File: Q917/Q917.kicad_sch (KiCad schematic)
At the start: 6 parts, among them J1 Analog, J2 Digital

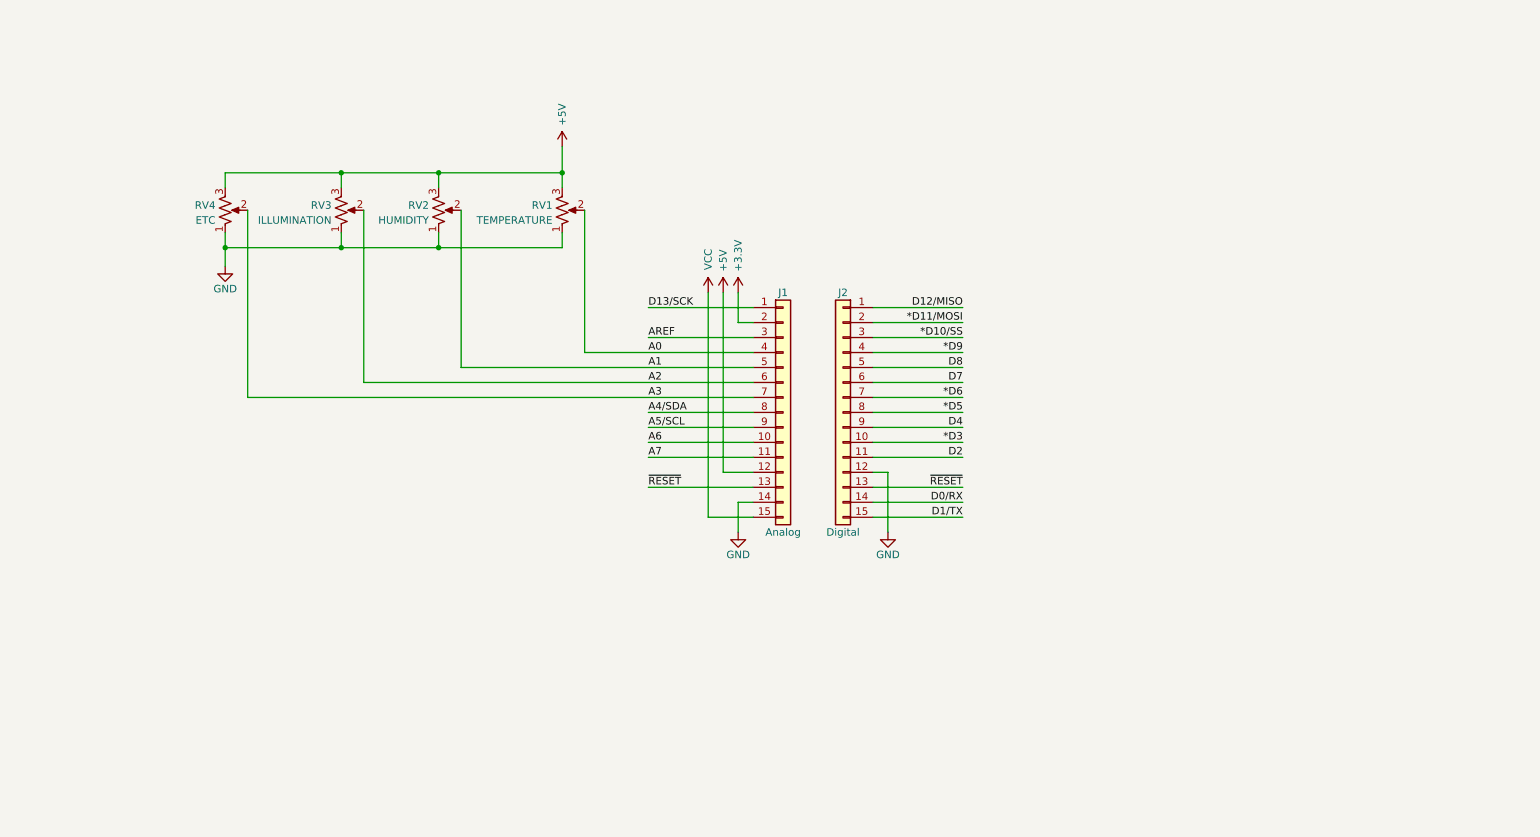
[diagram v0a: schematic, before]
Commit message: sche: コネクタ類に変更
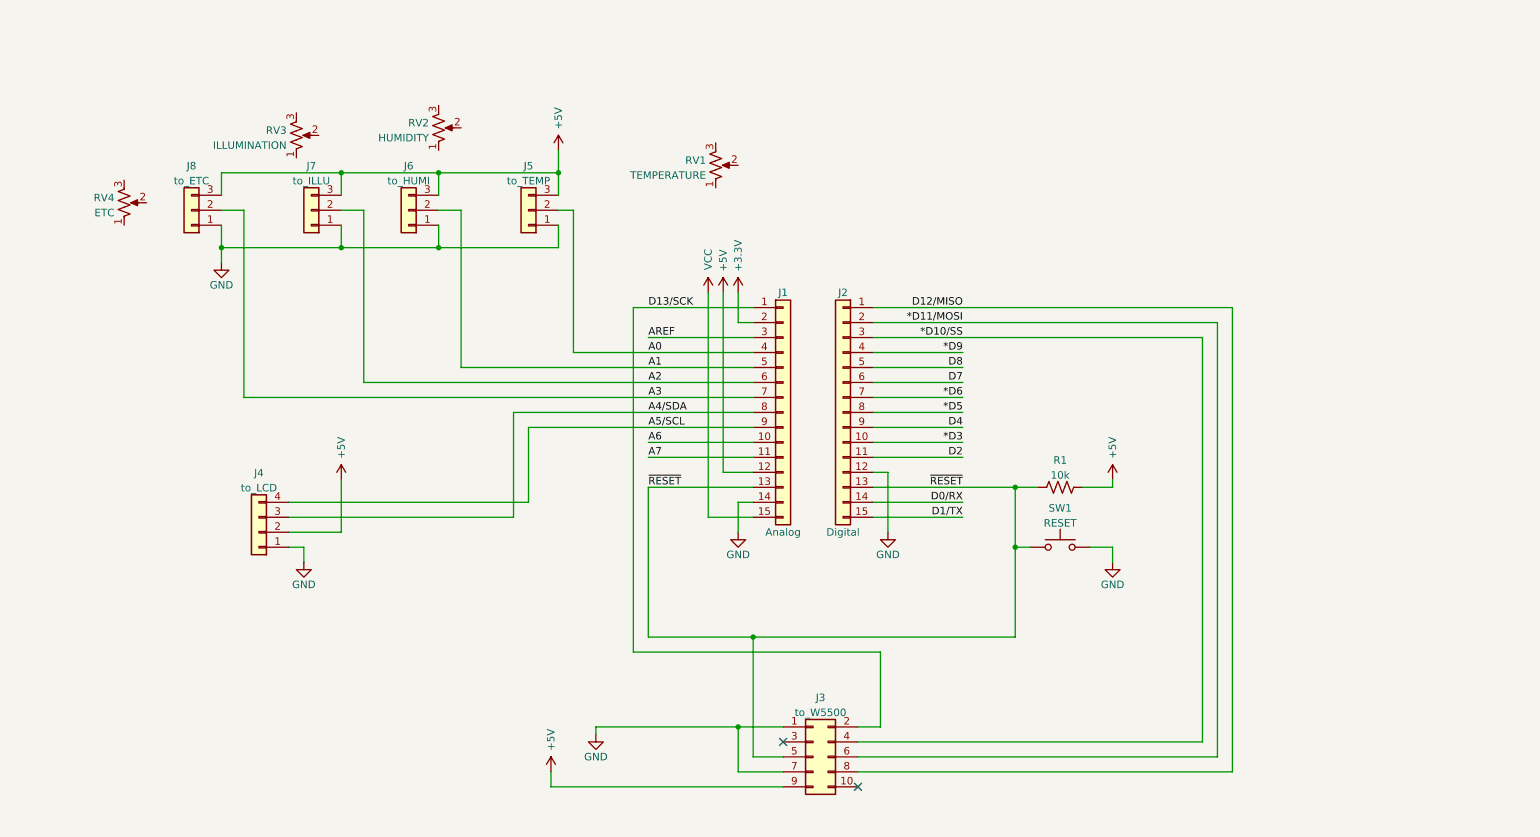
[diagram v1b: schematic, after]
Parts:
- added J3: to_W5500, Connector_PinHeader_2.54mm:PinHeader_2x05_P2.54mm_Vertical, symbol Connector_Generic:Conn_02x05_Odd_Even
- added J4: to_LCD, symbol Connector_Generic:Conn_01x04
- added J5: to_TEMP, Connector_JST:JST_XH_B3B-XH-A_1x03_P2.50mm_Vertical, symbol Connector_Generic:Conn_01x03
- added J6: to_HUMI, Connector_JST:JST_XH_B3B-XH-A_1x03_P2.50mm_Vertical, symbol Connector_Generic:Conn_01x03
- added J7: to_ILLU, Connector_JST:JST_XH_B3B-XH-A_1x03_P2.50mm_Vertical, symbol Connector_Generic:Conn_01x03
- added J8: to_ETC, Connector_JST:JST_XH_B3B-XH-A_1x03_P2.50mm_Vertical, symbol Connector_Generic:Conn_01x03
- added R1: 10k, symbol Device:R_US
- added SW1: RESET, symbol Switch:SW_Push
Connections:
- net *D10/SS: now also J3.4 (Pin_4)
- net *D11/MOSI: now also J3.6 (Pin_6)
- net +5V: now also J3.9 (Pin_9), J4.2 (Pin_2), J5.3 (Pin_3), J6.3 (Pin_3), J7.3 (Pin_3), J8.3 (Pin_3), R1.2; no longer RV1.3, RV2.3, RV3.3, RV4.3
- net A0: now also J5.2 (Pin_2); no longer RV1.2
- net A1: now also J6.2 (Pin_2); no longer RV2.2
- net A2: now also J7.2 (Pin_2); no longer RV3.2
- net A3: now also J8.2 (Pin_2); no longer RV4.2
- net A4/SDA: now also J4.3 (Pin_3)
- net A5/SCL: now also J4.4 (Pin_4)
- net D12/MISO: now also J3.8 (Pin_8)
- net D13/SCK: now also J3.2 (Pin_2)
- net GND: now also J3.1 (Pin_1), J3.7 (Pin_7), J4.1 (Pin_1), J5.1 (Pin_1), J6.1 (Pin_1), J7.1 (Pin_1), J8.1 (Pin_1), SW1.2; no longer RV1.1, RV2.1, RV3.1, RV4.1
- net ~{RESET}: now also J3.5 (Pin_5), R1.1, SW1.1
- no-connect marks 0 -> 2
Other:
- moved on the sheet: RV1, RV2, RV3, RV4

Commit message: sche: 初版完成
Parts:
- added C1: 100uF/25V, symbol Device:C_Polarized_Small
- added J10: HUMI_POT, symbol Connector:Conn_01x03_Male
- added J11: ILLUMI_POT, symbol Connector:Conn_01x03_Male
- added J12: ETC_POT, symbol Connector:Conn_01x03_Male
- added J13: DC5V, Connector_BarrelJack:BarrelJack_Horizontal, symbol Connector:Jack-DC
- added J9: TEMP_POT, symbol Connector:Conn_01x03_Male
- J1, J2: footprint Connector_PinHeader_2.54mm:PinHeader_1x15_P2.54mm_Vertical -> Connector_PinSocket_2.54mm:PinSocket_1x15_P2.54mm_Vertical
- J3: footprint Connector_PinHeader_2.54mm:PinHeader_2x05_P2.54mm_Vertical -> Connector_PinSocket_2.54mm:PinSocket_2x05_P2.54mm_Vertical
- J4: footprint (none) -> Connector_JST:JST_XH_B4B-XH-A_1x04_P2.50mm_Vertical
- R1: footprint (none) -> Resistor_THT:R_Axial_DIN0204_L3.6mm_D1.6mm_P7.62mm_Horizontal
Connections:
- net +5V: now also C1.1, J13.1
- net GND: now also C1.2, J13.2
- net at RV1.1: now also J9.1 (Pin_1)
- net at RV1.2: now also J9.2 (Pin_2)
- net at RV1.3: now also J9.3 (Pin_3)
- net at RV3.1: now also J11.1 (Pin_1)
- net at RV3.2: now also J11.2 (Pin_2)
- net at RV3.3: now also J11.3 (Pin_3)
- net at RV2.1: now also J10.1 (Pin_1)
- net at RV2.2: now also J10.2 (Pin_2)
- net at RV2.3: now also J10.3 (Pin_3)
- net at RV4.1: now also J12.1 (Pin_1)
- net at RV4.2: now also J12.2 (Pin_2)
- net at RV4.3: now also J12.3 (Pin_3)
- no-connect marks 2 -> 15
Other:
- moved on the sheet: RV1, RV2, RV3, RV4

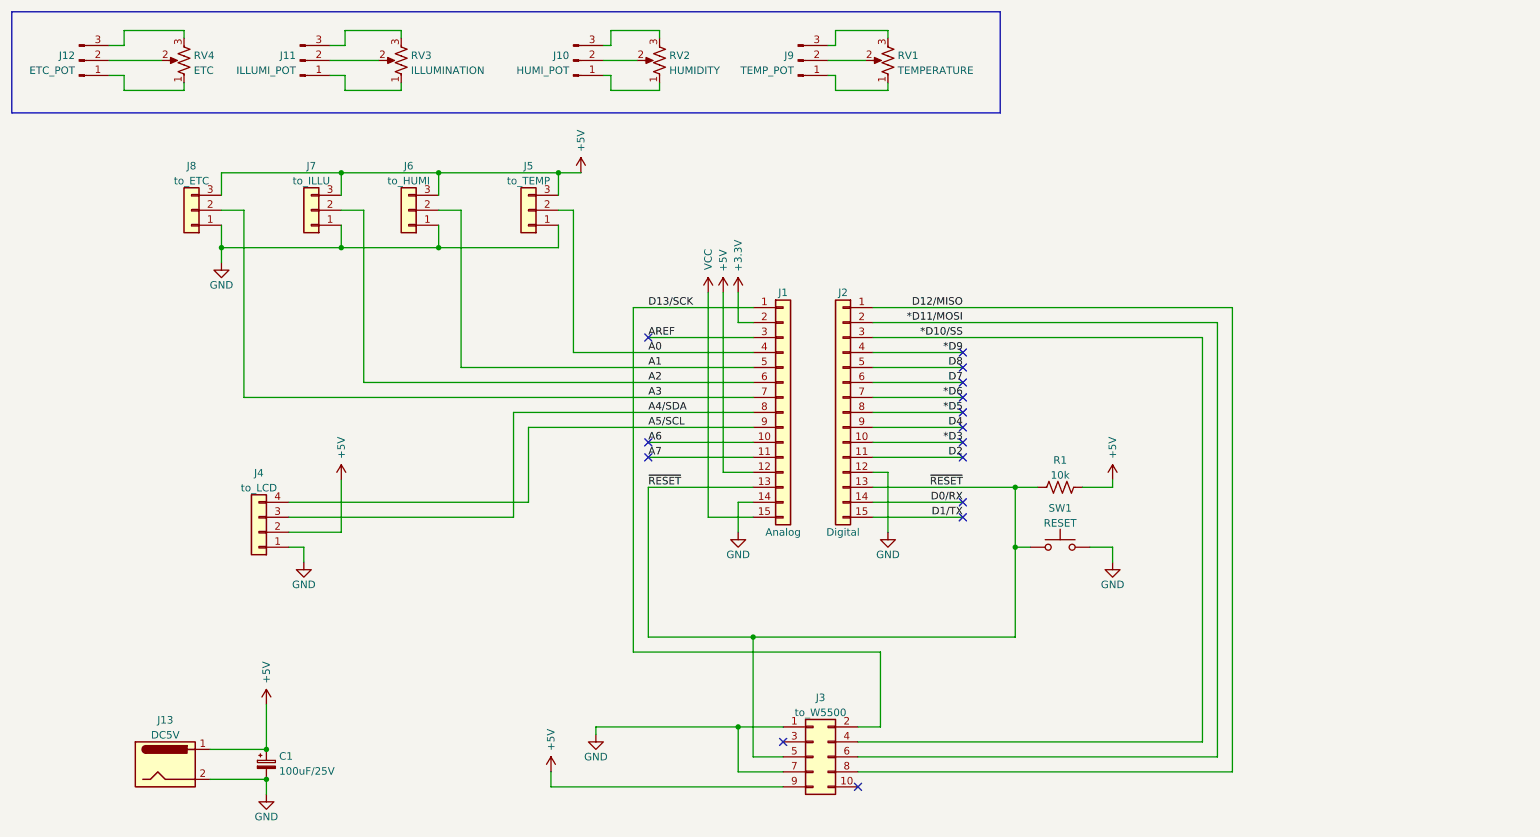
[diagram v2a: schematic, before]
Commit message: sche: PCB配線開始
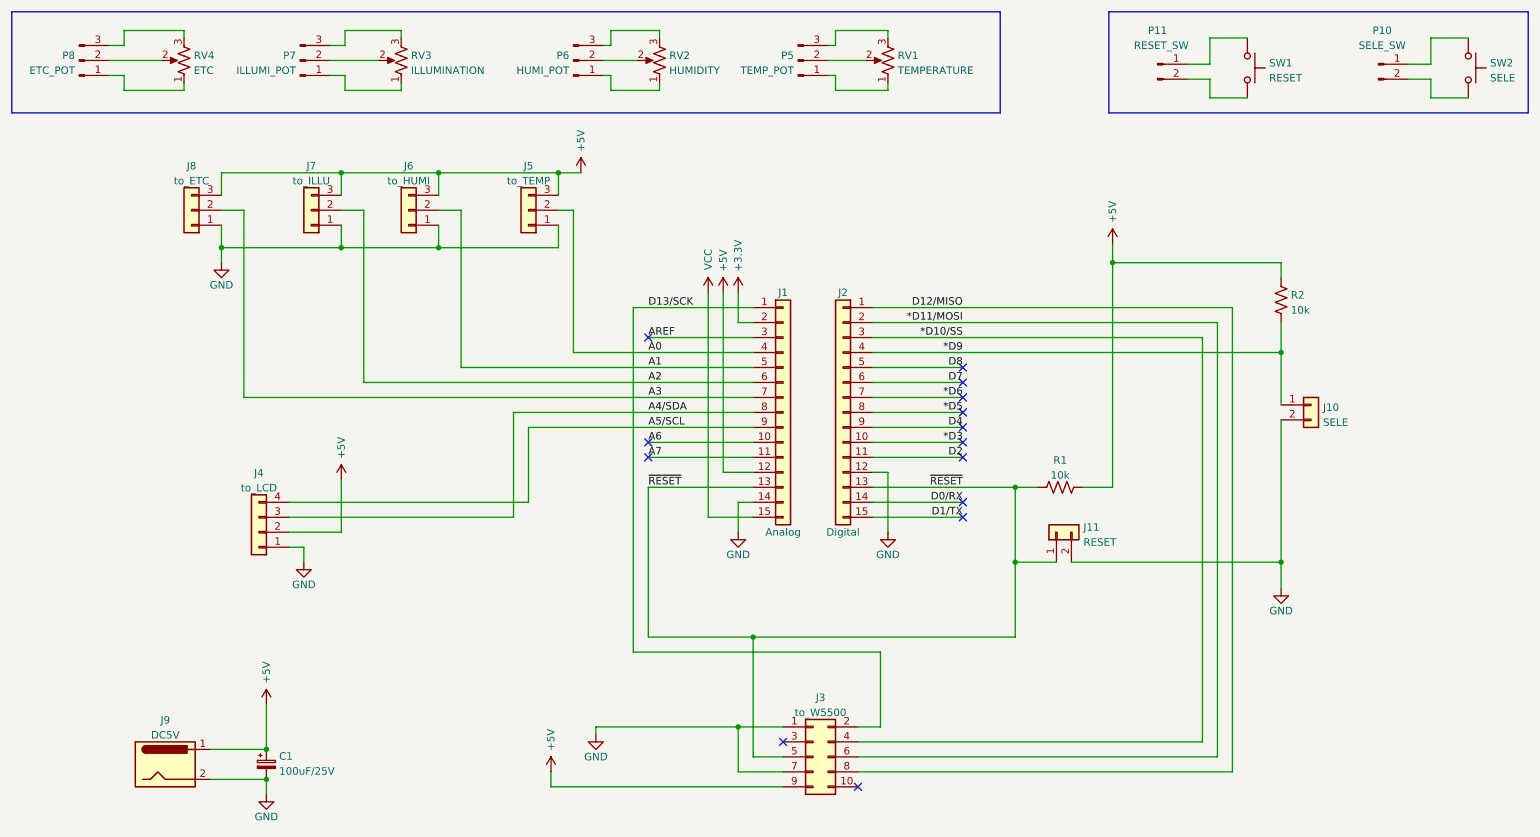
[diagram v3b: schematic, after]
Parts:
- added J10: SELE, Connector_JST:JST_XH_B2B-XH-A_1x02_P2.50mm_Vertical, symbol Connector_Generic:Conn_01x02
- added J11: RESET, Connector_JST:JST_XH_B2B-XH-A_1x02_P2.50mm_Vertical, symbol Connector_Generic:Conn_01x02
- added P10: SELE_SW, symbol Connector:Conn_01x02_Male
- added P11: RESET_SW, symbol Connector:Conn_01x02_Male
- added R2: 10k, Resistor_THT:R_Axial_DIN0204_L3.6mm_D1.6mm_P7.62mm_Horizontal, symbol Device:R_US
- added SW2: SELE, symbol Switch:SW_Push
- renumbered J13 to J9, J9 to P5, J10 to P6, J11 to P7, J12 to P8
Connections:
- net *D9: now also J10.1 (Pin_1), R2.1
- net +5V: now also R2.2
- net GND: now also J10.2 (Pin_2), J11.2 (Pin_2); no longer SW1.2
- net ~{RESET}: now also J11.1 (Pin_1); no longer SW1.1
- new net: P11.1 (Pin_1), SW1.1
- new net: P11.2 (Pin_2), SW1.2
- new net: P10.1 (Pin_1), SW2.1
- new net: P10.2 (Pin_2), SW2.2
- no-connect marks 15 -> 14
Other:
- moved on the sheet: SW1
